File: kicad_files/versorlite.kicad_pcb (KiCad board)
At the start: 4 copper layers, 33 x 81.3 mm, 135 parts, among them J1 Conn_01x01_Socket, J10 IGN_2, J3 RFD900ux 10 Pin Header, J4 Conn_ARM_JTAG_SWD_10, J5 RFD900ux 3 Pin Power Select, J6 USB_C_Receptacle_USB2.0_16P, J7 Micro_SD_Card_Det2, J8 Conn_01x02_Socket, J9 IGN_1, Q1 FDMC510P-MS, Q2 AO3400A, Q3 AO3400A, U1 STM32F407VGTx, U10 W25Q128JVS, U11 LT1963AxST-3.3, U12 AP63205WU, U13 74LVC1G125, U2 MS5611-01BA, U3 BMI088, U4 MMC5983MA, U5 MAX-M10S, U6 BMP388, U7 LSM6DSM, U9 WE-TVS-82400102, Y1 LFXTAL036869Reel 8MHz Crystal

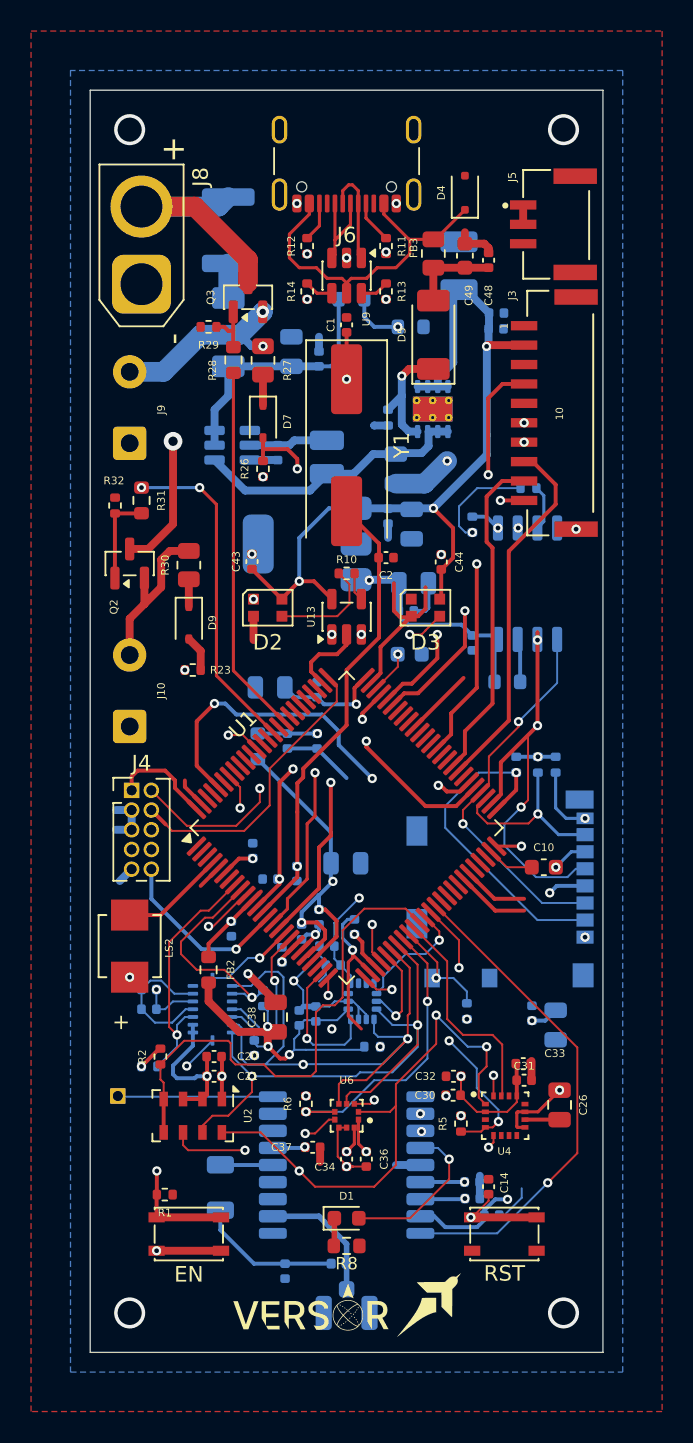
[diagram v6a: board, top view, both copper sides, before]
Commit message: add dedicated power switching
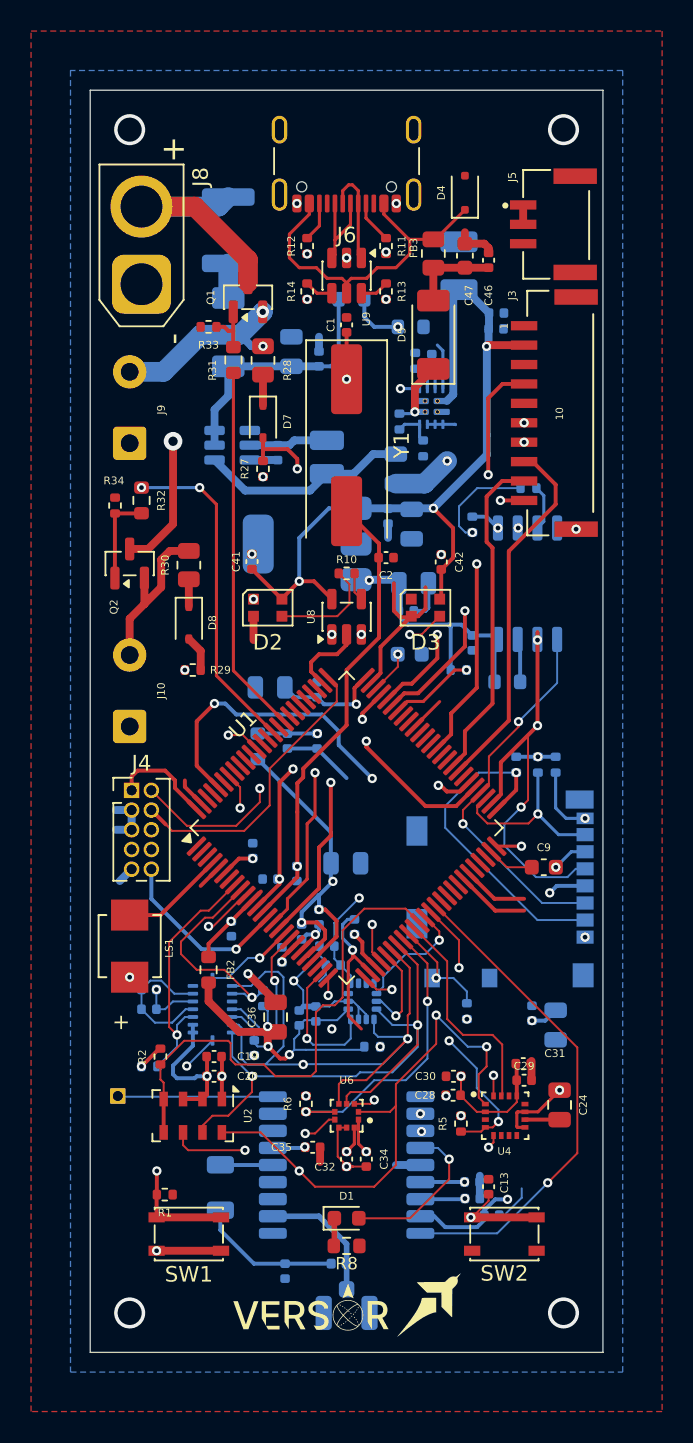
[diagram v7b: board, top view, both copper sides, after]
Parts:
- removed the Q1 at (149.1, 82.8)
- added C51: 100nf, Capacitor_SMD:C_0402_1005Metric, B.Cu at (149.0, 79.7)
- added R23: 33kΩ 1% tol, Resistor_SMD:R_0402_1005Metric, B.Cu at (147.9, 79.7)
- added R24: 100kΩ, Resistor_SMD:R_0402_1005Metric, B.Cu at (148.4, 85.3)
- added R35: 10kΩ, Resistor_SMD:R_0402_1005Metric, B.Cu at (150.7, 99.6)
- added U12: ~, footprints:IC_TPS2121RUXR, B.Cu at (149.0, 82.6)
- R22: value 10k -> 330kΩ
- moved R22 0.78 mm to (146.9, 83.6), turned to 90 degrees
- renumbered C11 to C10, C12 to C11, C13 to C12, C14 to C13, C15 to C14, C16 to C15, C17 to C16, C18 to C17, C19 to C18, C20 to C19, C21 to C20, C22 to C21, C23 to C22, C25 to C23, C26 to C24, C27 to C25, C28 to C26, C29 to C27, C30 to C28, C31 to C29, C4 to C3, C32 to C30, C33 to C31, C34 to C32, C35 to C33, C36 to C34, C37 to C35, C38 to C36, C39 to C37, C40 to C38, C41 to C39, C5 to C4, C42 to C40, C43 to C41, C44 to C42, C45 to C43, C46 to C44, C47 to C45, C48 to C46, C49 to C47, C50 to C48, C51 to C49, C6 to C5, C52 to C50, C53 to C52, C54 to C53, C55 to C54, C56 to C55, C58 to C56, C60 to C57, C61 to C58, C62 to C59, C7 to C6, C8 to C7, C9 to C8, C10 to C9, D8 to D6, D9 to D8, U.FL to J2, LS2 to LS1, Q3 to Q1, R24 to R25, R25 to R26, R26 to R27, R27 to R28, R23 to R29, R28 to R31, R31 to R32, R29 to R33, R32 to R34, EN to SW1, RST to SW2, U12 to U13, U13 to U8
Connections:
- R22 pad 1: /Power/+VBUS -> /Power/PR1
- R22 pad 2: GND -> /Power/+VBUS
- U1 pad 69: unconnected-(U1-PA10-Pad69) -> /MCU/POWER_STATUS
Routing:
- net /MCU/POWER_STATUS: track 0.00 -> 27.0 mm, vias 0 -> 2
- net Net-(U12-IN2): track 17.9 -> 13.5 mm
- net GND: track 120.6 -> 124.5 mm
- net /Power/+VBUS: track 7.88 -> 4.41 mm
- net +3.3V_MAIN: track 108.2 -> 111.2 mm
- net /Power/PR1: track 0.00 -> 2.57 mm
- net /MCU/PWM_TIM8_CHN4: track 4.47 -> 2.31 mm
- net Net-(U12-ILIM): track 0.00 -> 1.81 mm
- net Net-(U12-SS): track 0.00 -> 1.44 mm
- net +5V: track 53.8 -> 52.5 mm
- net /MCU/OSC_IN: track 49.8 -> 51.0 mm

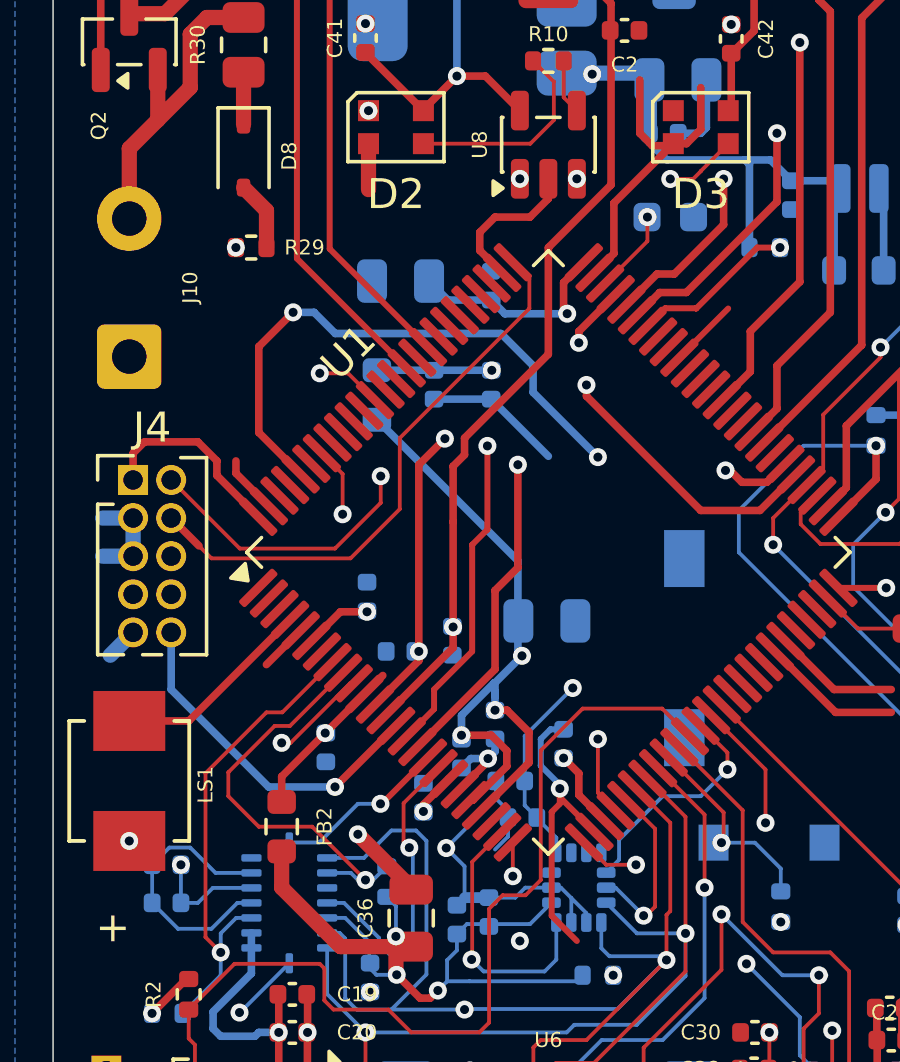
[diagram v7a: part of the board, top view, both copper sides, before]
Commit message: add ign_adc2
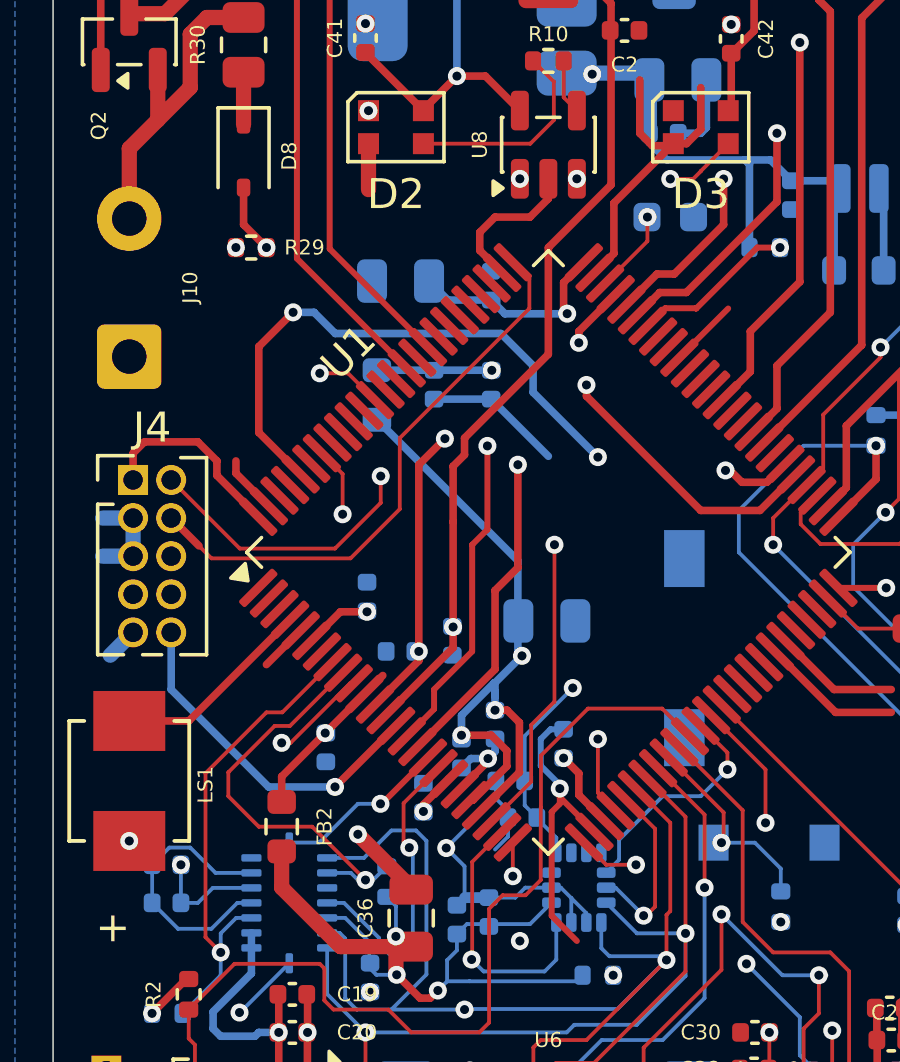
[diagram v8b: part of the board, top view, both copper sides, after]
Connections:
- net /MCU/IGN_ADC renamed /MCU/IGN_ADC1
- D8 pad 2: Net-(D8-A) -> /MCU/IGN_ADC2
- R29 pad 2: Net-(D8-A) -> /MCU/IGN_ADC2
- U1 pad 23: unconnected-(U1-PA0-Pad23) -> /MCU/IGN_ADC2
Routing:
- net /MCU/IGN_ADC2: track 0.00 -> 31.4 mm, vias 0 -> 2
- net Net-(D8-A): track 2.31 -> 0.00 mm
